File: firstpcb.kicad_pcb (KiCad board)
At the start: 2 copper layers, 24 parts, among them SW1 SW_Push, U1 ATmega32U4-AU, Y1 16MHz

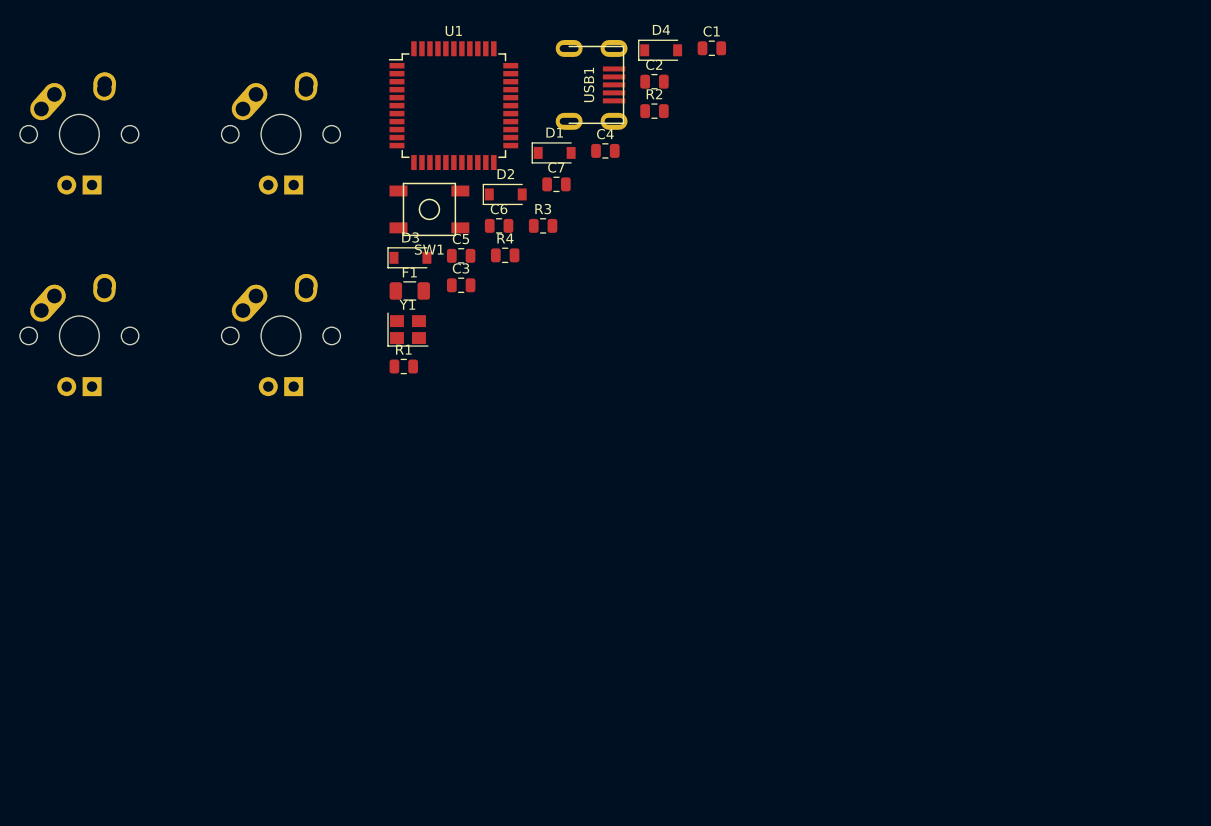
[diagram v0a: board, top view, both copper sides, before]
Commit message: d1-d4 placed on switches
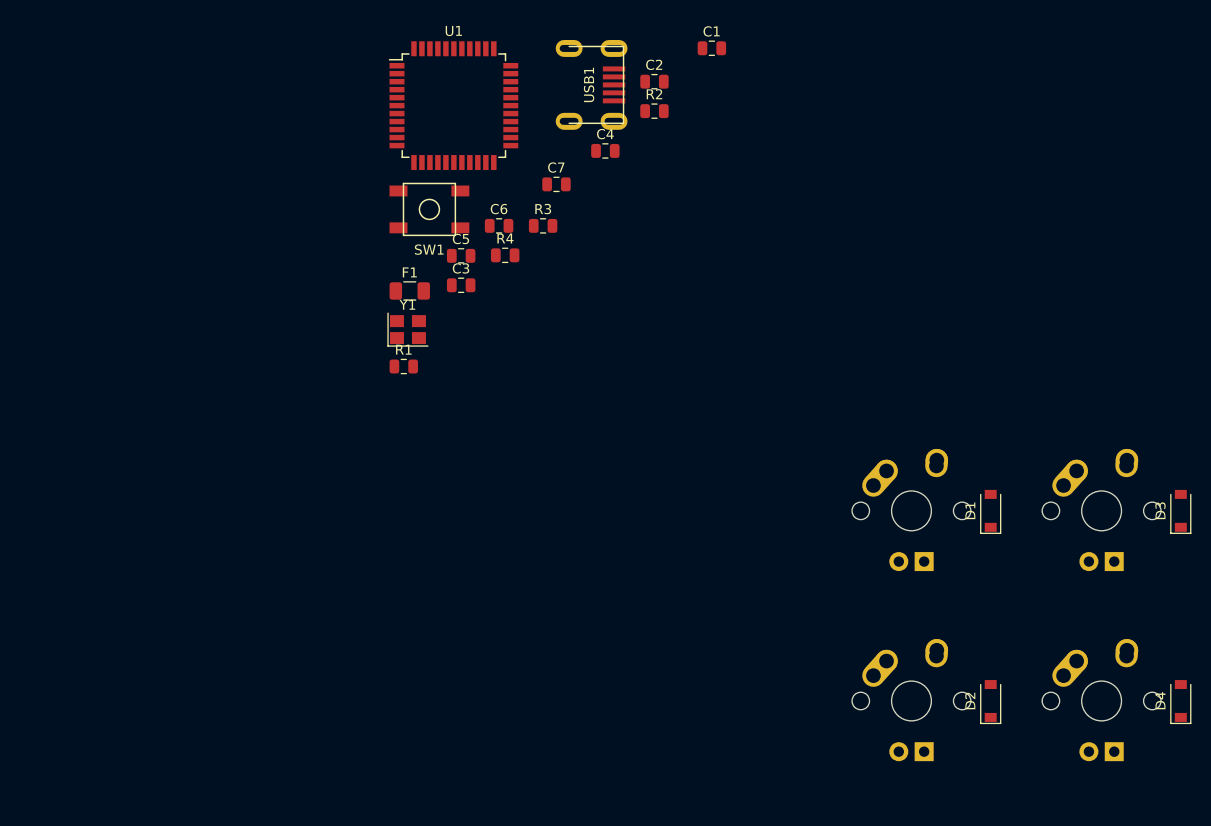
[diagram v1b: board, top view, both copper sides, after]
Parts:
- moved MX2 103.9 mm to (227.0, 104.8)
- moved MX4 99.9 mm to (227.0, 123.8)
- moved MX1 91.5 mm to (208.0, 104.8)
- moved D4 83.4 mm to (234.9, 123.8), turned to 90 degrees
- moved D3 81.2 mm to (234.9, 104.8), turned to 90 degrees
- moved MX3 73.0 mm to (208.0, 123.8)
- moved D2 70.3 mm to (215.9, 123.8), turned to 90 degrees
- moved D1 56.5 mm to (215.9, 104.8), turned to 90 degrees
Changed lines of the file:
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@@
   )
   (module MX_Alps_Hybrid:MX-1U (layer F.Cu)
-    (at 144.785 67.045)
+    (at 227.0125 123.825)
     (fp_text reference MX4 (at 0 3.175) (layer Dwgs.User)
       (effects (font (size 1 1) (thickness 0.15)))
@@
   )
   (module MX_Alps_Hybrid:MX-1U (layer F.Cu)
-    (at 144.785 87.245)
+    (at 207.9625 123.825)
     (fp_text reference MX3 (at 0 3.175) (layer Dwgs.User)
       (effects (font (size 1 1) (thickness 0.15)))
@@
   )
   (module MX_Alps_Hybrid:MX-1U (layer F.Cu)
-    (at 124.585 87.245)
+    (at 227.0125 104.775)
     (fp_text reference MX2 (at 0 3.175) (layer Dwgs.User)
       (effects (font (size 1 1) (thickness 0.15)))
@@
   )
   (module MX_Alps_Hybrid:MX-1U (layer F.Cu)
-    (at 124.585 67.045)
+    (at 207.9625 104.775)
     (fp_text reference MX1 (at 0 3.175) (layer Dwgs.User)
       (effects (font (size 1 1) (thickness 0.15)))
@@
   )
   (module Diode_SMD:D_SOD-123 (layer F.Cu)
-    (at 182.88 58.62)
+    (at 234.95 123.825 90)
     (descr SOD-123)
     (tags SOD-123)
     (attr smd)
-    (fp_text reference D4 (at 0 -2) (layer F.SilkS)
-      (effects (font (size 1 1) (thickness 0.15)))
-    )
-    (fp_text value SOD-123 (at 0 2.1) (layer F.Fab)
+    (fp_text reference D4 (at 0 -2 90) (layer F.SilkS)
+      (effects (font (size 1 1) (thickness 0.15)))
+    )
+    (fp_text value SOD-123 (at 0 2.1 90) (layer F.Fab)
       (effects (font (size 1 1) (thickness 0.15)))
     )
@@
     (fp_line (start 0.25 0) (end 0.75 0) (layer F.Fab) (width 0.1))
     (fp_line (start -2.25 -1) (end -2.25 1) (layer F.SilkS) (width 0.12))
-    (fp_text user %R (at 0 -2) (layer F.Fab)
-      (effects (font (size 1 1) (thickness 0.15)))
-    )
-    (pad 2 smd rect (at 1.65 0) (size 0.9 1.2) (layers F.Cu F.Paste F.Mask)
+    (fp_text user %R (at 0 -2 90) (layer F.Fab)
+      (effects (font (size 1 1) (thickness 0.15)))
+    )
+    (pad 2 smd rect (at 1.65 0 90) (size 0.9 1.2) (layers F.Cu F.Paste F.Mask)
       (net 10 "Net-(D4-Pad2)"))
-    (pad 1 smd rect (at -1.65 0) (size 0.9 1.2) (layers F.Cu F.Paste F.Mask)
+    (pad 1 smd rect (at -1.65 0 90) (size 0.9 1.2) (layers F.Cu F.Paste F.Mask)
       (net 8 ROW1))
     (model ${KISYS3DMOD}/Diode_SMD.3dshapes/D_SOD-123.wrl
@@
   )
   (module Diode_SMD:D_SOD-123 (layer F.Cu)
-    (at 157.76 79.42)
+    (at 234.95 104.775 90)
     (descr SOD-123)
     (tags SOD-123)
     (attr smd)
-    (fp_text reference D3 (at 0 -2) (layer F.SilkS)
-      (effects (font (size 1 1) (thickness 0.15)))
-    )
-    (fp_text value SOD-123 (at 0 2.1) (layer F.Fab)
+    (fp_text reference D3 (at 0 -2 90) (layer F.SilkS)
+      (effects (font (size 1 1) (thickness 0.15)))
+    )
+    (fp_text value SOD-123 (at 0 2.1 90) (layer F.Fab)
       (effects (font (size 1 1) (thickness 0.15)))
     )
@@
     (fp_line (start 0.25 0) (end 0.75 0) (layer F.Fab) (width 0.1))
     (fp_line (start -2.25 -1) (end -2.25 1) (layer F.SilkS) (width 0.12))
-    (fp_text user %R (at 0 -2) (layer F.Fab)
-      (effects (font (size 1 1) (thickness 0.15)))
-    )
-    (pad 2 smd rect (at 1.65 0) (size 0.9 1.2) (layers F.Cu F.Paste F.Mask)
+    (fp_text user %R (at 0 -2 90) (layer F.Fab)
+      (effects (font (size 1 1) (thickness 0.15)))
+    )
+    (pad 2 smd rect (at 1.65 0 90) (size 0.9 1.2) (layers F.Cu F.Paste F.Mask)
       (net 9 "Net-(D3-Pad2)"))
-    (pad 1 smd rect (at -1.65 0) (size 0.9 1.2) (layers F.Cu F.Paste F.Mask)
+    (pad 1 smd rect (at -1.65 0 90) (size 0.9 1.2) (layers F.Cu F.Paste F.Mask)
       (net 6 ROW0))
     (model ${KISYS3DMOD}/Diode_SMD.3dshapes/D_SOD-123.wrl
@@
   )
   (module Diode_SMD:D_SOD-123 (layer F.Cu)
-    (at 167.31 73.07)
+    (at 215.9 123.825 90)
     (descr SOD-123)
     (tags SOD-123)
     (attr smd)
-    (fp_text reference D2 (at 0 -2) (layer F.SilkS)
-      (effects (font (size 1 1) (thickness 0.15)))
-    )
-    (fp_text value SOD-123 (at 0 2.1) (layer F.Fab)
+    (fp_text reference D2 (at 0 -2 90) (layer F.SilkS)
+      (effects (font (size 1 1) (thickness 0.15)))
+    )
+    (fp_text value SOD-123 (at 0 2.1 90) (layer F.Fab)
       (effects (font (size 1 1) (thickness 0.15)))
     )
@@
     (fp_line (start 0.25 0) (end 0.75 0) (layer F.Fab) (width 0.1))
     (fp_line (start -2.25 -1) (end -2.25 1) (layer F.SilkS) (width 0.12))
-    (fp_text user %R (at 0 -2) (layer F.Fab)
-      (effects (font (size 1 1) (thickness 0.15)))
-    )
-    (pad 2 smd rect (at 1.65 0) (size 0.9 1.2) (layers F.Cu F.Paste F.Mask)
+    (fp_text user %R (at 0 -2 90) (layer F.Fab)
+      (effects (font (size 1 1) (thickness 0.15)))
+    )
+    (pad 2 smd rect (at 1.65 0 90) (size 0.9 1.2) (layers F.Cu F.Paste F.Mask)
       (net 7 "Net-(D2-Pad2)"))
-    (pad 1 smd rect (at -1.65 0) (size 0.9 1.2) (layers F.Cu F.Paste F.Mask)
+    (pad 1 smd rect (at -1.65 0 90) (size 0.9 1.2) (layers F.Cu F.Paste F.Mask)
       (net 8 ROW1))
     (model ${KISYS3DMOD}/Diode_SMD.3dshapes/D_SOD-123.wrl
@@
   )
   (module Diode_SMD:D_SOD-123 (layer F.Cu)
-    (at 172.21 68.91)
+    (at 215.9 104.775 90)
     (descr SOD-123)
     (tags SOD-123)
     (attr smd)
-    (fp_text reference D1 (at 0 -2) (layer F.SilkS)
-      (effects (font (size 1 1) (thickness 0.15)))
-    )
-    (fp_text value SOD-123 (at 0 2.1) (layer F.Fab)
+    (fp_text reference D1 (at 0 -2 90) (layer F.SilkS)
+      (effects (font (size 1 1) (thickness 0.15)))
+    )
+    (fp_text value SOD-123 (at 0 2.1 90) (layer F.Fab)
       (effects (font (size 1 1) (thickness 0.15)))
     )
@@
     (fp_line (start 0.25 0) (end 0.75 0) (layer F.Fab) (width 0.1))
     (fp_line (start -2.25 -1) (end -2.25 1) (layer F.SilkS) (width 0.12))
-    (fp_text user %R (at 0 -2) (layer F.Fab)
-      (effects (font (size 1 1) (thickness 0.15)))
-    )
-    (pad 2 smd rect (at 1.65 0) (size 0.9 1.2) (layers F.Cu F.Paste F.Mask)
+    (fp_text user %R (at 0 -2 90) (layer F.Fab)
+      (effects (font (size 1 1) (thickness 0.15)))
+    )
+    (pad 2 smd rect (at 1.65 0 90) (size 0.9 1.2) (layers F.Cu F.Paste F.Mask)
       (net 5 "Net-(D1-Pad2)"))
-    (pad 1 smd rect (at -1.65 0) (size 0.9 1.2) (layers F.Cu F.Paste F.Mask)
+    (pad 1 smd rect (at -1.65 0 90) (size 0.9 1.2) (layers F.Cu F.Paste F.Mask)
       (net 6 ROW0))
     (model ${KISYS3DMOD}/Diode_SMD.3dshapes/D_SOD-123.wrl

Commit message: Little bit of routing done
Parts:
- moved C1 64.8 mm to (188.0, 123.2), turned to 90 degrees
- moved SW1 55.8 mm to (171.3, 129.2)
- moved C4 54.6 mm to (180.3, 123.2), turned to 90 degrees
- moved U1 53.6 mm to (184.2, 113.0)
- moved C2 49.9 mm to (193.0, 110.5), turned to 90 degrees
- moved C5 47.3 mm to (193.0, 115.6), turned to 90 degrees
- moved Y1 45.3 mm to (184.2, 123.2)
- moved R2 44.0 mm to (170.7, 107.2), turned to 90 degrees
- moved C7 40.2 mm to (162.7, 111.1), turned to 90 degrees
- moved C3 36.8 mm to (175.3, 116.8), turned to 90 degrees
- moved C6 35.9 mm to (189.2, 104.1)
- moved USB1 34.9 mm to (172.9, 97.0), turned to 270 degrees
- moved R4 32.3 mm to (172.2, 111.1), turned to 90 degrees
- moved R3 31.1 mm to (174.6, 107.2), turned to 90 degrees
- moved F1 31.0 mm to (181.0, 103.2), turned to 180 degrees
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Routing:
- net VCC: track 0.00 -> 6.86 mm
- net D+: track 0.00 -> 5.65 mm
- net D-: track 0.00 -> 5.10 mm
- net GND: track 0.00 -> 0.88 mm
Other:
- net class Default: trace_width 0.25 -> 0.254
- net class Power added: clearance 0.2, trace_width 0.381, via_dia 0.8, via_drill 0.4
